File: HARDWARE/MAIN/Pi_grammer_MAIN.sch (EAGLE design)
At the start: 56 parts, among them J3 TARGET_copy, Q1 220mA/50V/3.5Ω, Q2 220mA/50V/3.5Ω, Q3 220mA/50V/3.5Ω, Q4 220mA/50V/3.5Ω, Q5 220mA/50V/3.5Ω, U1 AT42QT1010UDFN, U2 74LVC4066

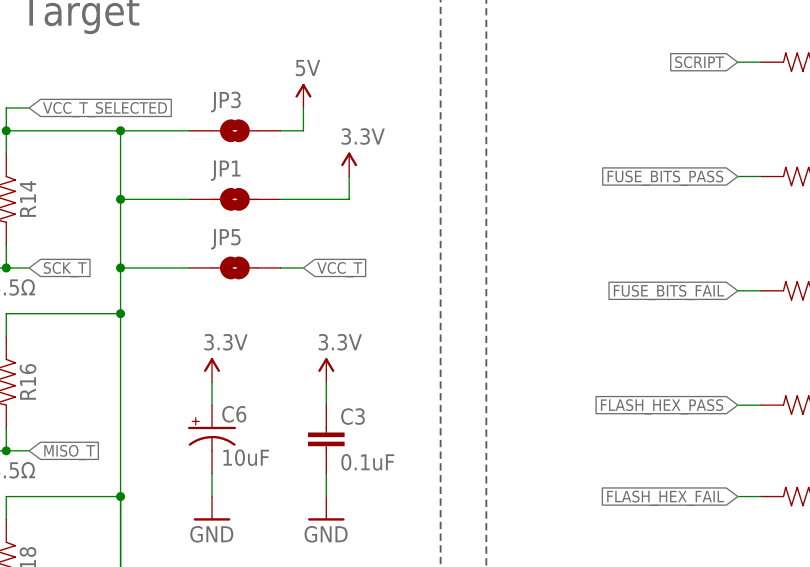
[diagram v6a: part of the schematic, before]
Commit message: Swapped out package to paste-closed jumper for TARGET VCC
This needed a default target logic select. It is now closed (selected) via paste on the "TARGET VCC" option.
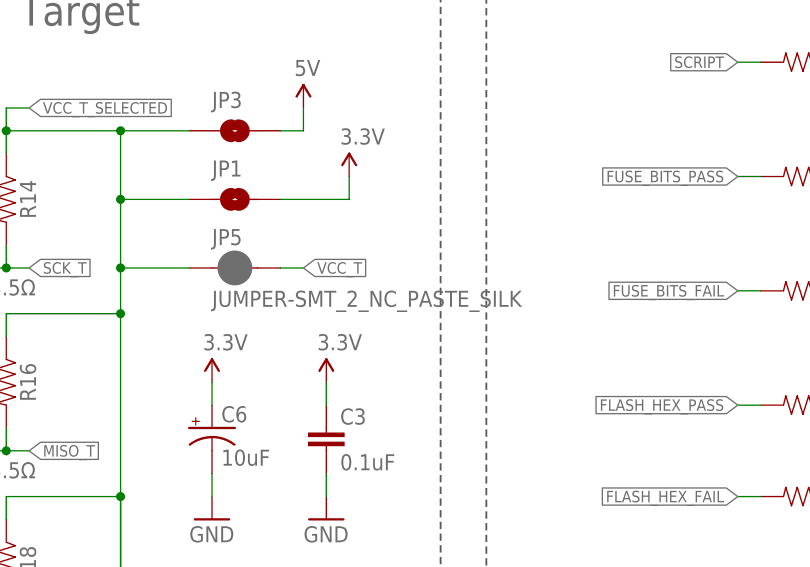
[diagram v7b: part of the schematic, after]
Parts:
- JP5: value JUMPER-SMT_2_NO_SILK -> JUMPER-SMT_2_NC_PASTE_SILK; device SparkFun-Jumpers:JUMPER-SMT_2_NO_SILK -> SparkFun-Jumpers:JUMPER-SMT_2_NC_PASTE_SILK
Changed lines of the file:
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@@
 <?xml version="1.0" encoding="utf-8"?>
 <!DOCTYPE eagle SYSTEM "eagle.dtd">
-<eagle version="6.5.0">
+<eagle version="7.6.0">
 <drawing>
 <settings>
@@
 <grid distance="0.1" unitdist="inch" unit="inch" style="lines" multiple="1" display="no" altdistance="0.01" altunitdist="inch" altunit="inch"/>
 <layers>
-<layer number="1" name="Top" color="4" fill="1" visible="no" active="no"/>
-<layer number="2" name="Route2" color="1" fill="3" visible="no" active="no"/>
-<layer number="3" name="Route3" color="4" fill="3" visible="no" active="no"/>
-<layer number="4" name="Route4" color="1" fill="4" visible="no" active="no"/>
-<layer number="5" name="Route5" color="4" fill="4" visible="no" active="no"/>
-<layer number="6" name="Route6" color="1" fill="8" visible="no" active="no"/>
-<layer number="7" name="Route7" color="4" fill="8" visible="no" active="no"/>
-<layer number="8" name="Route8" color="1" fill="2" visible="no" active="no"/>
-<layer number="9" name="Route9" color="4" fill="2" visible="no" active="no"/>
-<layer number="10" name="Route10" color="1" fill="7" visible="no" active="no"/>
-<layer number="11" name="Route11" color="4" fill="7" visible="no" active="no"/>
-<layer number="12" name="Route12" color="1" fill="5" visible="no" active="no"/>
-<layer number="13" name="Route13" color="4" fill="5" visible="no" active="no"/>
-<layer number="14" name="Route14" color="1" fill="6" visible="no" active="no"/>
-<layer number="15" name="Route15" color="4" fill="6" visible="no" active="no"/>
-<layer number="16" name="Bottom" color="1" fill="1" visible="no" active="no"/>
-<layer number="17" name="Pads" color="2" fill="1" visible="no" active="no"/>
-<layer number="18" name="Vias" color="2" fill="1" visible="no" active="no"/>
-<layer number="19" name="Unrouted" color="6" fill="1" visible="no" active="no"/>
-<layer number="20" name="Dimension" color="15" fill="1" visible="no" active="no"/>
-<layer number="21" name="tPlace" color="16" fill="1" visible="no" active="no"/>
-<layer number="22" name="bPlace" color="14" fill="1" visible="no" active="no"/>
-<layer number="23" name="tOrigins" color="15" fill="1" visible="no" active="no"/>
-<layer number="24" name="bOrigins" color="15" fill="1" visible="no" active="no"/>
-<layer number="25" name="tNames" color="7" fill="1" visible="no" active="no"/>
-<layer number="26" name="bNames" color="7" fill="1" visible="no" active="no"/>
-<layer number="27" name="tValues" color="7" fill="1" visible="no" active="no"/>
-<layer number="28" name="bValues" color="7" fill="1" visible="no" active="no"/>
+<layer number="1" name="Top" color="4" fill="1" visible="yes" active="no"/>
+<layer number="2" name="Route2" color="1" fill="3" visible="yes" active="no"/>
+<layer number="3" name="Route3" color="4" fill="3" visible="yes" active="no"/>
+<layer number="4" name="Route4" color="1" fill="4" visible="yes" active="no"/>
+<layer number="5" name="Route5" color="4" fill="4" visible="yes" active="no"/>
+<layer number="6" name="Route6" color="1" fill="8" visible="yes" active="no"/>
+<layer number="7" name="Route7" color="4" fill="8" visible="yes" active="no"/>
+<layer number="8" name="Route8" color="1" fill="2" visible="yes" active="no"/>
+<layer number="9" name="Route9" color="4" fill="2" visible="yes" active="no"/>
+<layer number="10" name="Route10" color="1" fill="7" visible="yes" active="no"/>
+<layer number="11" name="Route11" color="4" fill="7" visible="yes" active="no"/>
+<layer number="12" name="Route12" color="1" fill="5" visible="yes" active="no"/>
+<layer number="13" name="Route13" color="4" fill="5" visible="yes" active="no"/>
+<layer number="14" name="Route14" color="1" fill="6" visible="yes" active="no"/>
+<layer number="15" name="Route15" color="4" fill="6" visible="yes" active="no"/>
+<layer number="16" name="Bottom" color="1" fill="1" visible="yes" active="no"/>
+<layer number="17" name="Pads" color="2" fill="1" visible="yes" active="no"/>
+<layer number="18" name="Vias" color="2" fill="1" visible="yes" active="no"/>
+<layer number="19" name="Unrouted" color="6" fill="1" visible="yes" active="no"/>
+<layer number="20" name="Dimension" color="15" fill="1" visible="yes" active="no"/>
+<layer number="21" name="tPlace" color="16" fill="1" visible="yes" active="no"/>
+<layer number="22" name="bPlace" color="14" fill="1" visible="yes" active="no"/>
+<layer number="23" name="tOrigins" color="15" fill="1" visible="yes" active="no"/>
+<layer number="24" name="bOrigins" color="15" fill="1" visible="yes" active="no"/>
+<layer number="25" name="tNames" color="7" fill="1" visible="yes" active="no"/>
+<layer number="26" name="bNames" color="7" fill="1" visible="yes" active="no"/>
+<layer number="27" name="tValues" color="7" fill="1" visible="yes" active="no"/>
+<layer number="28" name="bValues" color="7" fill="1" visible="yes" active="no"/>
 <layer number="29" name="tStop" color="7" fill="3" visible="no" active="no"/>
 <layer number="30" name="bStop" color="7" fill="6" visible="no" active="no"/>
@@
 <layer number="35" name="tGlue" color="7" fill="4" visible="no" active="no"/>
 <layer number="36" name="bGlue" color="7" fill="5" visible="no" active="no"/>
-<layer number="37" name="tTest" color="7" fill="1" visible="no" active="no"/>
-<layer number="38" name="bTest" color="7" fill="1" visible="no" active="no"/>
+<layer number="37" name="tTest" color="7" fill="1" visible="yes" active="no"/>
+<layer number="38" name="bTest" color="7" fill="1" visible="yes" active="no"/>
 <layer number="39" name="tKeepout" color="4" fill="11" visible="no" active="no"/>
 <layer number="40" name="bKeepout" color="1" fill="11" visible="no" active="no"/>
@@
 <layer number="44" name="Drills" color="7" fill="1" visible="no" active="no"/>
 <layer number="45" name="Holes" color="7" fill="1" visible="no" active="no"/>
-<layer number="46" name="Milling" color="3" fill="1" visible="no" active="no"/>
-<layer number="47" name="Measures" color="7" fill="1" visible="no" active="no"/>
-<layer number="48" name="Document" color="7" fill="1" visible="no" active="no"/>
-<layer number="49" name="Reference" color="7" fill="1" visible="no" active="no"/>
-<layer number="50" name="dxf" color="7" fill="1" visible="no" active="no"/>
-<layer number="51" name="tDocu" color="6" fill="1" visible="no" active="no"/>
-<layer number="52" name="bDocu" color="7" fill="1" visible="no" active="no"/>
-<layer number="53" name="tGND_GNDA" color="7" fill="9" visible="no" active="no"/>
-<layer number="54" name="bGND_GNDA" color="1" fill="9" visible="no" active="no"/>
-<layer number="56" name="wert" color="7" fill="1" visible="no" active="no"/>
-<layer number="57" name="tCAD" color="7" fill="1" visible="no" active="no"/>
-<layer number="59" name="tCarbon" color="7" fill="1" visible="no" active="no"/>
-<layer number="60" name="bCarbon" color="7" fill="1" visible="no" active="no"/>
+<layer number="46" name="Milling" color="3" fill="1" visible="yes" active="no"/>
+<layer number="47" name="Measures" color="7" fill="1" visible="yes" active="no"/>
+<layer number="48" name="Document" color="7" fill="1" visible="yes" active="no"/>
+<layer number="49" name="Reference" color="13" fill="1" visible="yes" active="no"/>
+<layer number="50" name="dxf" color="7" fill="1" visible="yes" active="no"/>
+<layer number="51" name="tDocu" color="6" fill="1" visible="yes" active="no"/>
+<layer number="52" name="bDocu" color="7" fill="1" visible="yes" active="no"/>
+<layer number="53" name="tGND_GNDA" color="7" fill="9" visible="yes" active="no"/>
+<layer number="54" name="bGND_GNDA" color="1" fill="9" visible="yes" active="no"/>
+<layer number="56" name="wert" color="7" fill="1" visible="yes" active="no"/>
+<layer number="57" name="tCAD" color="7" fill="1" visible="yes" active="no"/>
+<layer number="59" name="tCarbon" color="7" fill="1" visible="yes" active="no"/>
+<layer number="60" name="bCarbon" color="7" fill="1" visible="yes" active="no"/>
 <layer number="90" name="Modules" color="5" fill="1" visible="yes" active="yes"/>
 <layer number="91" name="Nets" color="2" fill="1" visible="yes" active="yes"/>
@@
 <part name="R17" library="SparkFun-Resistors" deviceset="10KOHM" device="-0603-1/10W-1%" value="10k"/>
 <part name="R18" library="SparkFun-Resistors" deviceset="10KOHM" device="-0603-1/10W-1%" value="10k"/>
-<part name="JP5" library="SparkFun-Jumpers" deviceset="JUMPER-SMT_2_NO" device="_SILK" value=""/>
+<part name="JP5" library="SparkFun-Jumpers" deviceset="JUMPER-SMT_2_NC_PASTE" device="_SILK" value="JUMPER-SMT_2_NC_PASTE_SILK"/>
 <part name="SUPPLY5" library="SparkFun-Aesthetics" deviceset="3.3V" device=""/>
 <part name="JP1" library="SparkFun-Jumpers" deviceset="JUMPER-SMT_2_NO" device="_SILK" value=""/>

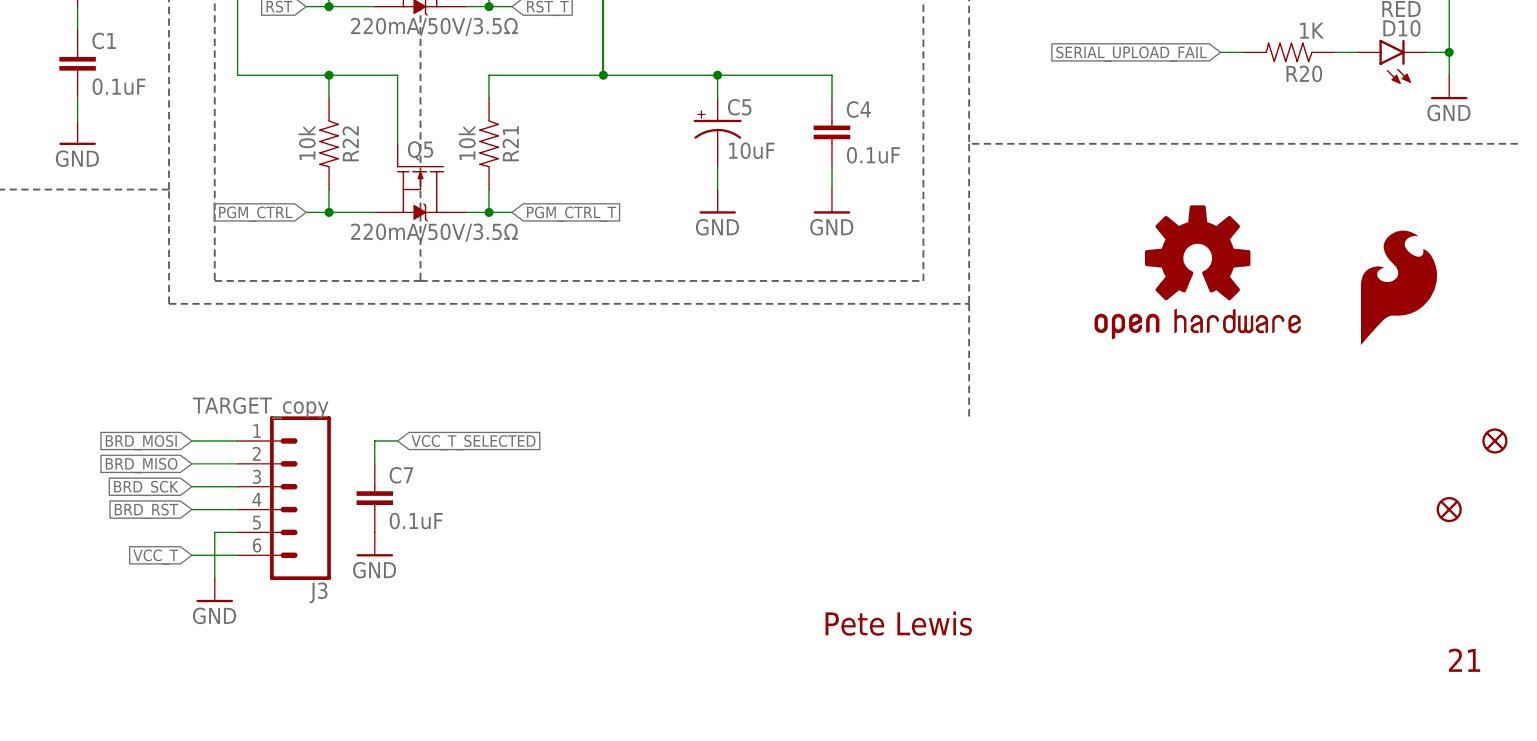
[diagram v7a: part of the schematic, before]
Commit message: pi_grammer_MAIN updates for storefront product
-moved to RA SMT 1x6 header for programming lines to cable, had to re-route a few things, MISO and MOSI have a much better direct route now.
-Enlarged most silk to standard 0.05
-changed text silk on "blank boxes" to more generic use case terms - project name, version, date etc.
-added prod ID to switch IC
-updated copper and sch version number to v22
-added large sparkfun logo to bottom side silk
-removed passive component values silk - this is only used during QC testing hardware assembly (when we build them by hand)
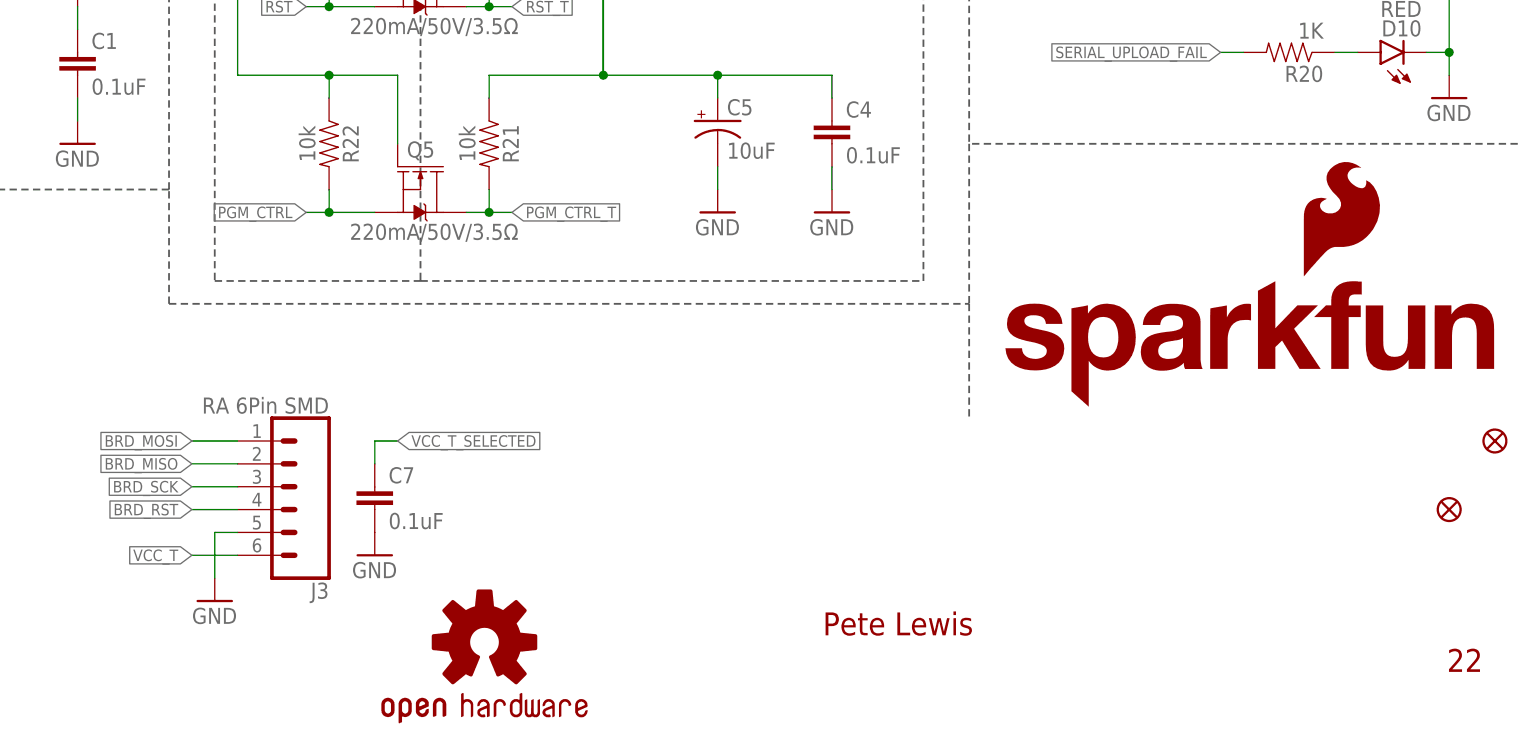
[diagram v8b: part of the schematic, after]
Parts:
- added LOGO3: SFE_LOGO_NAME.6_INCH, SparkFun-Aesthetics:SFE_LOGO_NAME.6_INCH
- J3: value TARGET_copy -> RA 6Pin SMD; device SparkFun-Connectors:CONN_06LOCK -> SparkFun-Connectors:CONN_06SMD
- LOGO2: value OSHW-LOGOS -> OSHW-LOGOL; device SparkFun-Aesthetics:OSHW-LOGOS -> SparkFun-Aesthetics:OSHW-LOGOL
- U2: PROD_ID (none) -> IC-13944
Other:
- note added: "22"
- note removed: "21"
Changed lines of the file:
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@@
 <part name="R8" library="SparkFun-Resistors" deviceset="1KOHM-1/10W-1%(0603)" device="" value="1K"/>
 <part name="D7" library="SparkFun-LED" deviceset="LED-GREEN" device="1206" value="GREEN"/>
-<part name="LOGO2" library="SparkFun-Aesthetics" deviceset="OSHW-LOGO" device="S" value="OSHW-LOGOS"/>
+<part name="LOGO2" library="SparkFun-Aesthetics" deviceset="OSHW-LOGO" device="L" value="OSHW-LOGOL"/>
 <part name="U1" library="Testing" deviceset="AT42QT1010" device="UDFN">
 <attribute name="PROD_ID" value="IC-11778"/>
@@
 <part name="C7" library="SparkFun-Capacitors" deviceset="0.1UF" device="-0603-25V-(+80/-20%)" value="0.1uF"/>
 <part name="GND10" library="SparkFun" deviceset="GND" device=""/>
-<part name="U2" library="Testing" deviceset="74LVC4066_MUX_1:1_X4" device="" value="74LVC4066"/>
+<part name="U2" library="Testing" deviceset="74LVC4066_MUX_1:1_X4" device="" value="74LVC4066">
+<attribute name="PROD_ID" value="IC-13944"/>
+</part>
 <part name="GND12" library="SparkFun" deviceset="GND" device=""/>
-<part name="J3" library="SparkFun-Connectors" deviceset="CONN_06" device="LOCK" value="TARGET_copy">
+<part name="J3" library="SparkFun-Connectors" deviceset="CONN_06" device="SMD" value="RA 6Pin SMD">
 <attribute name="PROD_ID" value="CONN-10140"/>
 </part>
@@
 <part name="R21" library="SparkFun-Resistors" deviceset="10KOHM" device="-0603-1/10W-1%" value="10k"/>
 <part name="R22" library="SparkFun-Resistors" deviceset="10KOHM" device="-0603-1/10W-1%" value="10k"/>
+<part name="LOGO3" library="SparkFun-Aesthetics" deviceset="SFE_LOGO_NAME" device=".6_INCH" value="SFE_LOGO_NAME.6_INCH"/>
 </parts>
 <sheets>
@@
 <text x="12.7" y="363.22" size="2.54" layer="94" font="vector">Raspberry Pi 2x20 connector</text>
 <text x="179.324" y="194.31" size="2.54" layer="94" font="vector">Pete Lewis</text>
-<text x="248.666" y="190.246" size="2.54" layer="94" font="vector">21</text>
+<text x="248.666" y="190.246" size="2.54" layer="94" font="vector">22</text>
 <text x="203.2" y="363.22" size="2.54" layer="94" font="vector">Status LEDs</text>
 <text x="10.16" y="281.94" size="2.54" layer="94" font="vector">Capsense trigger</text>
@@
 <instance part="R8" gate="G$1" x="231.14" y="289.56" rot="R180"/>
 <instance part="D7" gate="G$1" x="241.3" y="289.56" rot="R90"/>
-<instance part="LOGO2" gate="G$1" x="220.98" y="236.22"/>
+<instance part="LOGO2" gate="G$1" x="141.732" y="193.548"/>
 <instance part="U1" gate="G$1" x="48.26" y="261.62">
 <attribute name="PROD_ID" x="48.26" y="261.62" size="1.27" layer="96" display="off"/>
@@
 <instance part="C5" gate="G$1" x="167.64" y="251.46"/>
 <instance part="GND8" gate="1" x="167.64" y="241.3"/>
-<instance part="LOGO1" gate="G$1" x="238.76" y="226.06"/>
+<instance part="LOGO1" gate="G$1" x="232.41" y="233.68"/>
 <instance part="C7" gate="G$1" x="129.54" y="208.28"/>
 <instance part="GND10" gate="1" x="129.54" y="203.2"/>
-<instance part="U2" gate="G$1" x="58.42" y="210.82"/>
+<instance part="U2" gate="G$1" x="58.42" y="210.82">
+<attribute name="PROD_ID" x="58.42" y="210.82" size="1.27" layer="96" display="off"/>
+</instance>
 <instance part="GND12" gate="1" x="40.64" y="193.04"/>
 <instance part="J3" gate="G$1" x="119.38" y="210.82" rot="R180">
@@
 <instance part="R21" gate="G$1" x="142.24" y="248.92" rot="R270"/>
 <instance part="R22" gate="G$1" x="124.46" y="248.92" rot="R270"/>
+<instance part="LOGO3" gate="G$1" x="197.612" y="219.71"/>
 </instances>
 <busses>
